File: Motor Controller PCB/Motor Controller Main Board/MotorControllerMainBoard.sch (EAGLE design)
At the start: 46 parts, among them T1 TEENSY_3.1_ALL_PINS

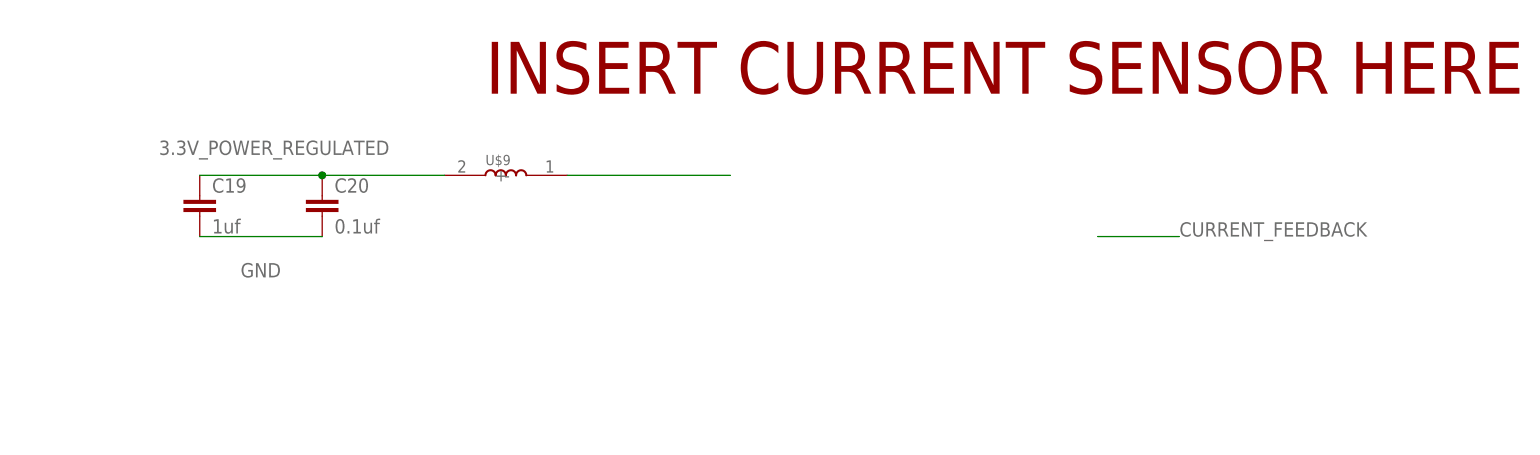
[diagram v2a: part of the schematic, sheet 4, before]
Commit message: Changes to current sensor LP filter
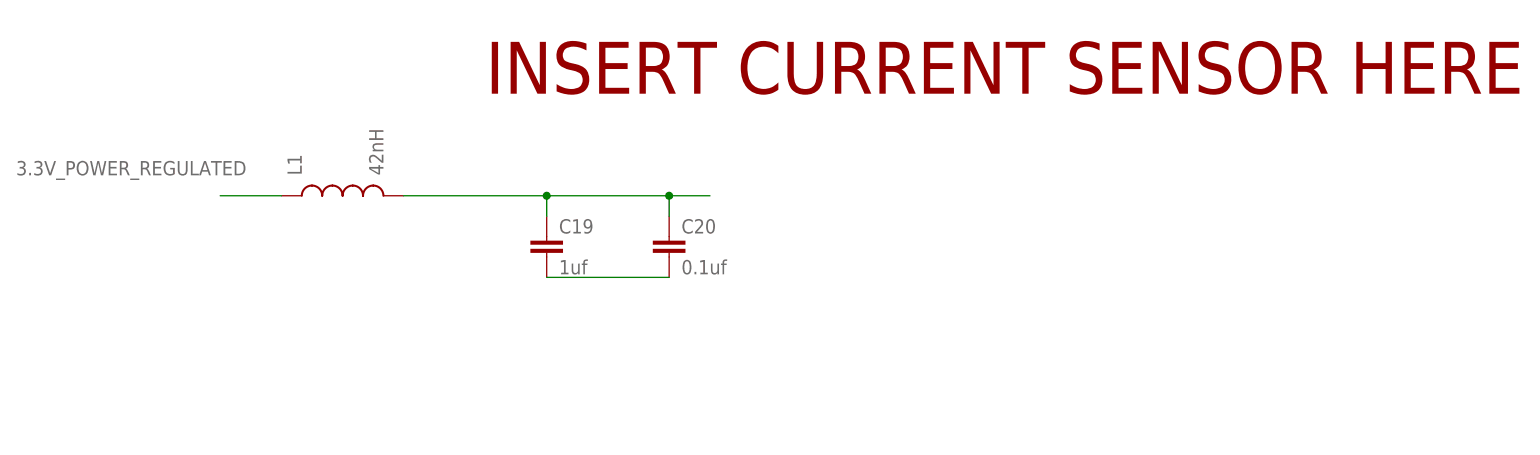
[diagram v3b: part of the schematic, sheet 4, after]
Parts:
- removed U$9: (no value), MotorControllerEagleLibrary:PA4320
- added L1: 42nH, SparkFun (2015_10_14 22_27_04 UTC):INDUCTOR0805
- U$10, U$7: value (none) -> 330uH
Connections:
- new net N$2: C19.2, C20.2
- net 3.3V_POWER_REGULATED: now also L1.1; no longer C19.1, C20.1, U$9.-
- net GND: no longer C19.2, C20.2
- net N$6: now also C19.1, C20.1, L1.2; no longer U$9.+
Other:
- note added: "12V Supply"
- note removed: "12V Variable Supply"
- moved on the sheet: C19, C20
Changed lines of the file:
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@@
 <?xml version="1.0" encoding="utf-8"?>
 <!DOCTYPE eagle SYSTEM "eagle.dtd">
-<eagle version="7.7.0">
+<eagle version="7.5.0">
 <drawing>
 <settings>
@@
 <part name="T1" library="Teensy_3_and_LC_Series_Boards_v1.1" deviceset="TEENSY_3.1_ALL_PINS" device=""/>
 <part name="U$5" library="MotorControllerEagleLibrary" deviceset="FLYBACK" device=""/>
-<part name="U$7" library="MotorControllerEagleLibrary" deviceset="PA4320" device=""/>
+<part name="U$7" library="MotorControllerEagleLibrary" deviceset="PA4320" device="" value="330uH"/>
 <part name="U$8" library="MotorControllerEagleLibrary" deviceset="1N5819" device=""/>
 <part name="C5" library="MotorControllerEagleLibrary" deviceset="EEUFR1H221B" device=""/>
@@
 <part name="C8" library="MotorControllerEagleLibrary" deviceset="EEUFR1H221B" device=""/>
 <part name="U$6" library="MotorControllerEagleLibrary" deviceset="TL2575HV-15IKTTR" device=""/>
-<part name="U$10" library="MotorControllerEagleLibrary" deviceset="PA4320" device=""/>
+<part name="U$10" library="MotorControllerEagleLibrary" deviceset="PA4320" device="" value="330uH"/>
 <part name="U$11" library="MotorControllerEagleLibrary" deviceset="1N5819" device=""/>
 <part name="C9" library="MotorControllerEagleLibrary" deviceset="EEUFR1H221B" device=""/>
@@
 <part name="C19" library="SparkFun-Capacitors" deviceset="CAP" device="0805" value="1uf"/>
 <part name="C20" library="SparkFun-Capacitors" deviceset="CAP" device="0805" value="0.1uf"/>
-<part name="U$9" library="MotorControllerEagleLibrary" deviceset="PA4320" device=""/>
 <part name="ENCODER_INPUT" library="con-molex-c-grid" deviceset="90130-1?06" device=""/>
 <part name="C21" library="SparkFun-Capacitors" deviceset="CAP" device="0805" value="0.1uf"/>
@@
 <part name="R3" library="SparkFun-Passives" deviceset="RESISTOR" device="0805-RES" value="3.3k"/>
 <part name="R4" library="SparkFun-Passives" deviceset="RESISTOR" device="0805-RES" value="3.3k"/>
+<part name="L1" library="SparkFun (2015_10_14 22_27_04 UTC)" deviceset="INDUCTOR" device="0805" value="42nH"/>
 </parts>
 <sheets>
@@
 <instance part="FRAME3" gate="G$1" x="0" y="0"/>
 <instance part="FRAME3" gate="G$2" x="172.72" y="0"/>
-<instance part="C19" gate="G$1" x="60.96" y="121.92"/>
-<instance part="C20" gate="G$1" x="76.2" y="121.92"/>
-<instance part="U$9" gate="PA4320_INDUCTOR" x="99.06" y="127"/>
+<instance part="C19" gate="G$1" x="104.14" y="116.84"/>
+<instance part="C20" gate="G$1" x="119.38" y="116.84"/>
+<instance part="L1" gate="G$1" x="78.74" y="124.46" rot="R90"/>
 </instances>
 <busses>
 </busses>
 <nets>
+<net name="N$6" class="0">
+<segment>
+<wire x1="86.36" y1="124.46" x2="104.14" y2="124.46" width="0.1524" layer="91"/>
+<pinref part="C19" gate="G$1" pin="1"/>
+<wire x1="104.14" y1="124.46" x2="119.38" y2="124.46" width="0.1524" layer="91"/>
+<wire x1="119.38" y1="124.46" x2="124.46" y2="124.46" width="0.1524" layer="91"/>
+<wire x1="104.14" y1="124.46" x2="104.14" y2="121.92" width="0.1524" layer="91"/>
+<junction x="104.14" y="124.46"/>
+<pinref part="C20" gate="G$1" pin="1"/>
+<wire x1="119.38" y1="124.46" x2="119.38" y2="121.92" width="0.1524" layer="91"/>
+<junction x="119.38" y="124.46"/>
+<pinref part="L1" gate="G$1" pin="2"/>
+</segment>
+</net>
+<net name="N$2" class="0">
+<segment>
+<pinref part="C19" gate="G$1" pin="2"/>
+<pinref part="C20" gate="G$1" pin="2"/>
+<wire x1="104.14" y1="114.3" x2="119.38" y2="114.3" width="0.1524" layer="91"/>
+</segment>
+</net>
 <net name="3.3V_POWER_REGULATED" class="0">
 <segment>
-<pinref part="C19" gate="G$1" pin="1"/>
-<pinref part="C20" gate="G$1" pin="1"/>
-<wire x1="60.96" y1="127" x2="76.2" y2="127" width="0.1524" layer="91"/>
-<wire x1="76.2" y1="127" x2="91.44" y2="127" width="0.1524" layer="91"/>
-<junction x="76.2" y="127"/>
-<pinref part="U$9" gate="PA4320_INDUCTOR" pin="-"/>
-<label x="55.88" y="129.54" size="1.778" layer="95"/>
-</segment>
-</net>
-<net name="N$6" class="0">
-<segment>
-<pinref part="U$9" gate="PA4320_INDUCTOR" pin="+"/>
-<wire x1="106.68" y1="127" x2="127" y2="127" width="0.1524" layer="91"/>
-</segment>
-</net>
-<net name="GND" class="0">
-<segment>
-<pinref part="C20" gate="G$1" pin="2"/>
-<pinref part="C19" gate="G$1" pin="2"/>
-<wire x1="76.2" y1="119.38" x2="60.96" y2="119.38" width="0.1524" layer="91"/>
-<label x="66.04" y="114.3" size="1.778" layer="95"/>
-</segment>
-</net>
-<net name="CURRENT_FEEDBACK" class="0">
-<segment>
-<wire x1="172.72" y1="119.38" x2="182.88" y2="119.38" width="0.1524" layer="91"/>
-<label x="182.88" y="119.38" size="1.778" layer="95"/>
+<pinref part="L1" gate="G$1" pin="1"/>
+<wire x1="71.12" y1="124.46" x2="63.5" y2="124.46" width="0.1524" layer="91"/>
+<label x="38.1" y="127" size="1.778" layer="95"/>
 </segment>
 </net>
@@
 <plain>
 <text x="200.66" y="27.94" size="3.81" layer="94">POWER SUPPLY</text>
-<text x="172.72" y="154.94" size="6.4516" layer="94">12V Variable Supply</text>
+<text x="172.72" y="154.94" size="6.4516" layer="94">12V Supply</text>
 <text x="172.72" y="83.82" size="6.4516" layer="94">5V Supply</text>
 <text x="58.42" y="149.86" size="1.27" layer="94">220uF Panasonic Caps</text>

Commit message: Added buffers
Choose a JFET op-amp for its ability to reject noise while having high
input impedance.

-Used a buffer for the output of the current sensor

-Used a 1/10 gain buffer to read the voltage of the supply voltage
safely.
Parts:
- added C23: 0.1uF, rcl:C-EUC0805
- added C24: (no value), rcl:C-EUC0805
- added C25: 1uF, rcl:C-EUC0805
- added R5, R6: 100k, rcl:R-US_R0805
- added R7, R8: 10k, rcl:R-US_R0805
- added U1: TL072CDT, MotorControllerEagleLibrary:TL072CDT
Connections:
- new net CURRENT_SENSOR_OUTPUT: U1.1IN+
- new net N$7: R5.2, R8.2, U1.2IN+
- new net N$9: R6.2, R7.1, U1.2IN-
- new net SUPPLY_VOLTAGE: C25.1, R7.2, T1.18/A4/T/SDA0, U1.2OUT
- net CURRENT_FEEDBACK: now also C23.1, U1.1IN-, U1.1OUT
- net GND: now also C23.2, C25.2, R6.1, R8.1
- net SAFE_POWER: now also R5.1
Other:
- note added: "2OUT = (R7+R8)/(R5+R6)Vin =~ 1/10*Vin"
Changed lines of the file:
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@@
 <part name="R4" library="SparkFun-Passives" deviceset="RESISTOR" device="0805-RES" value="3.3k"/>
 <part name="L1" library="SparkFun (2015_10_14 22_27_04 UTC)" deviceset="INDUCTOR" device="0805" value="42nH"/>
+<part name="U1" library="MotorControllerEagleLibrary" deviceset="TL072CDT" device=""/>
+<part name="C23" library="rcl" deviceset="C-EU" device="C0805" value="0.1uF"/>
+<part name="C24" library="rcl" deviceset="C-EU" device="C0805"/>
+<part name="GND9" library="E-P-008-R1.2" deviceset="GND" device=""/>
+<part name="R5" library="rcl" deviceset="R-US_" device="R0805" value="100k"/>
+<part name="R6" library="rcl" deviceset="R-US_" device="R0805" value="100k"/>
+<part name="R7" library="rcl" deviceset="R-US_" device="R0805" value="10k"/>
+<part name="R8" library="rcl" deviceset="R-US_" device="R0805" value="10k"/>
+<part name="GND10" library="E-P-008-R1.2" deviceset="GND" device=""/>
+<part name="C25" library="rcl" deviceset="C-EU" device="C0805" value="1uF"/>
+<part name="GND11" library="E-P-008-R1.2" deviceset="GND" device=""/>
+<part name="GND12" library="E-P-008-R1.2" deviceset="GND" device=""/>
 </parts>
 <sheets>
@@
 <text x="203.2" y="25.4" size="3.81" layer="94">TEENSY 3.2
 CONNECTIONS</text>
+<text x="195.58" y="43.18" size="1.778" layer="91">2OUT = (R7+R8)/(R5+R6)Vin =~ 1/10*Vin</text>
 </plain>
 <instances>
@@
 <instance part="R3" gate="G$1" x="43.18" y="50.8" rot="R90"/>
 <instance part="R4" gate="G$1" x="83.82" y="50.8" rot="R90"/>
+<instance part="U1" gate="A" x="190.5" y="68.58"/>
+<instance part="C23" gate="G$1" x="213.36" y="76.2"/>
+<instance part="C24" gate="G$1" x="294.64" y="76.2"/>
+<instance part="GND9" gate="1" x="213.36" y="68.58"/>
+<instance part="R5" gate="G$1" x="154.94" y="66.04"/>
+<instance part="R6" gate="G$1" x="154.94" y="55.88"/>
+<instance part="R7" gate="G$1" x="182.88" y="48.26"/>
+<instance part="R8" gate="G$1" x="165.1" y="48.26" rot="R90"/>
+<instance part="GND10" gate="1" x="165.1" y="40.64"/>
+<instance part="C25" gate="G$1" x="213.36" y="58.42"/>
+<instance part="GND11" gate="1" x="213.36" y="50.8"/>
+<instance part="GND12" gate="1" x="144.78" y="48.26"/>
 </instances>
 <busses>
@@
 <wire x1="60.96" y1="58.42" x2="58.42" y2="58.42" width="0.1524" layer="91"/>
 <label x="53.34" y="58.42" size="1.778" layer="95"/>
+</segment>
+<segment>
+<pinref part="C23" gate="G$1" pin="2"/>
+<pinref part="GND9" gate="1" pin="GND"/>
+</segment>
+<segment>
+<pinref part="R8" gate="G$1" pin="1"/>
+<pinref part="GND10" gate="1" pin="GND"/>
+</segment>
+<segment>
+<pinref part="C25" gate="G$1" pin="2"/>
+<pinref part="GND11" gate="1" pin="GND"/>
+</segment>
+<segment>
+<pinref part="R6" gate="G$1" pin="1"/>
+<wire x1="149.86" y1="55.88" x2="144.78" y2="55.88" width="0.1524" layer="91"/>
+<pinref part="GND12" gate="1" pin="GND"/>
+<wire x1="144.78" y1="55.88" x2="144.78" y2="50.8" width="0.1524" layer="91"/>
 </segment>
 </net>
@@
 <label x="88.9" y="127" size="1.778" layer="95"/>
 </segment>
+<segment>
+<pinref part="U1" gate="A" pin="1IN-"/>
+<wire x1="172.72" y1="81.28" x2="167.64" y2="81.28" width="0.1524" layer="91"/>
+<wire x1="167.64" y1="81.28" x2="167.64" y2="91.44" width="0.1524" layer="91"/>
+<wire x1="167.64" y1="91.44" x2="203.2" y2="91.44" width="0.1524" layer="91"/>
+<wire x1="203.2" y1="91.44" x2="203.2" y2="78.74" width="0.1524" layer="91"/>
+<pinref part="U1" gate="A" pin="1OUT"/>
+<wire x1="203.2" y1="78.74" x2="200.66" y2="78.74" width="0.1524" layer="91"/>
+<wire x1="203.2" y1="78.74" x2="213.36" y2="78.74" width="0.1524" layer="91"/>
+<junction x="203.2" y="78.74"/>
+<pinref part="C23" gate="G$1" pin="1"/>
+<junction x="213.36" y="78.74"/>
+<wire x1="213.36" y1="78.74" x2="226.06" y2="78.74" width="0.1524" layer="91"/>
+<label x="226.06" y="78.74" size="1.778" layer="95"/>
+</segment>
 </net>
 <net name="ENCODER_A" class="0">
@@
 </segment>
 </net>
+<net name="CURRENT_SENSOR_OUTPUT" class="0">
+<segment>
+<pinref part="U1" gate="A" pin="1IN+"/>
+<wire x1="172.72" y1="76.2" x2="160.02" y2="76.2" width="0.1524" layer="91"/>
+<label x="142.24" y="76.2" size="1.778" layer="95"/>
+</segment>
+</net>
+<net name="N$7" class="0">
+<segment>
+<pinref part="R5" gate="G$1" pin="2"/>
+<pinref part="U1" gate="A" pin="2IN+"/>
+<wire x1="160.02" y1="66.04" x2="165.1" y2="63.5" width="0.1524" layer="91"/>
+<pinref part="R8" gate="G$1" pin="2"/>
+<wire x1="165.1" y1="63.5" x2="172.72" y2="63.5" width="0.1524" layer="91"/>
+<wire x1="165.1" y1="63.5" x2="165.1" y2="53.34" width="0.1524" layer="91"/>
+<junction x="165.1" y="63.5"/>
+</segment>
+</net>
+<net name="N$9" class="0">
+<segment>
+<pinref part="R6" gate="G$1" pin="2"/>
+<pinref part="U1" gate="A" pin="2IN-"/>
+<wire x1="160.02" y1="55.88" x2="170.18" y2="58.42" width="0.1524" layer="91"/>
+<wire x1="170.18" y1="58.42" x2="172.72" y2="58.42" width="0.1524" layer="91"/>
+<wire x1="170.18" y1="58.42" x2="170.18" y2="48.26" width="0.1524" layer="91"/>
+<junction x="170.18" y="58.42"/>
+<pinref part="R7" gate="G$1" pin="1"/>
+<wire x1="170.18" y1="48.26" x2="177.8" y2="48.26" width="0.1524" layer="91"/>
+</segment>
+</net>
+<net name="SUPPLY_VOLTAGE" class="0">
+<segment>
+<pinref part="R7" gate="G$1" pin="2"/>
+<wire x1="187.96" y1="48.26" x2="203.2" y2="48.26" width="0.1524" layer="91"/>
+<wire x1="203.2" y1="48.26" x2="203.2" y2="60.96" width="0.1524" layer="91"/>
+<pinref part="U1" gate="A" pin="2OUT"/>
+<wire x1="203.2" y1="60.96" x2="200.66" y2="60.96" width="0.1524" layer="91"/>
+<wire x1="203.2" y1="60.96" x2="213.36" y2="60.96" width="0.1524" layer="91"/>
+<junction x="203.2" y="60.96"/>
+<pinref part="C25" gate="G$1" pin="1"/>
+<wire x1="213.36" y1="60.96" x2="226.06" y2="60.96" width="0.1524" layer="91"/>
+<junction x="213.36" y="60.96"/>
+<label x="226.06" y="60.96" size="1.778" layer="95"/>
+</segment>
+<segment>
+<pinref part="T1" gate="G$1" pin="18/A4/T/SDA0"/>
+<wire x1="116.84" y1="116.84" x2="114.3" y2="116.84" width="0.1524" layer="91"/>
+<label x="88.9" y="116.84" size="1.778" layer="95"/>
+</segment>
+</net>
+<net name="SAFE_POWER" class="0">
+<segment>
+<pinref part="R5" gate="G$1" pin="1"/>
+<wire x1="149.86" y1="66.04" x2="147.32" y2="66.04" width="0.1524" layer="91"/>
+<label x="134.62" y="66.04" size="1.778" layer="95"/>
+</segment>
+</net>
